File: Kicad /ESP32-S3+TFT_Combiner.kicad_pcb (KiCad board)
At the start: 2 copper layers, 98 x 55.9 mm, 6 parts, among them J1 Conn_01x04, J2 Conn_01x14, J3 Conn_01x22, J4 Conn_01x22, J5 Conn_01x22, J6 Conn_01x22

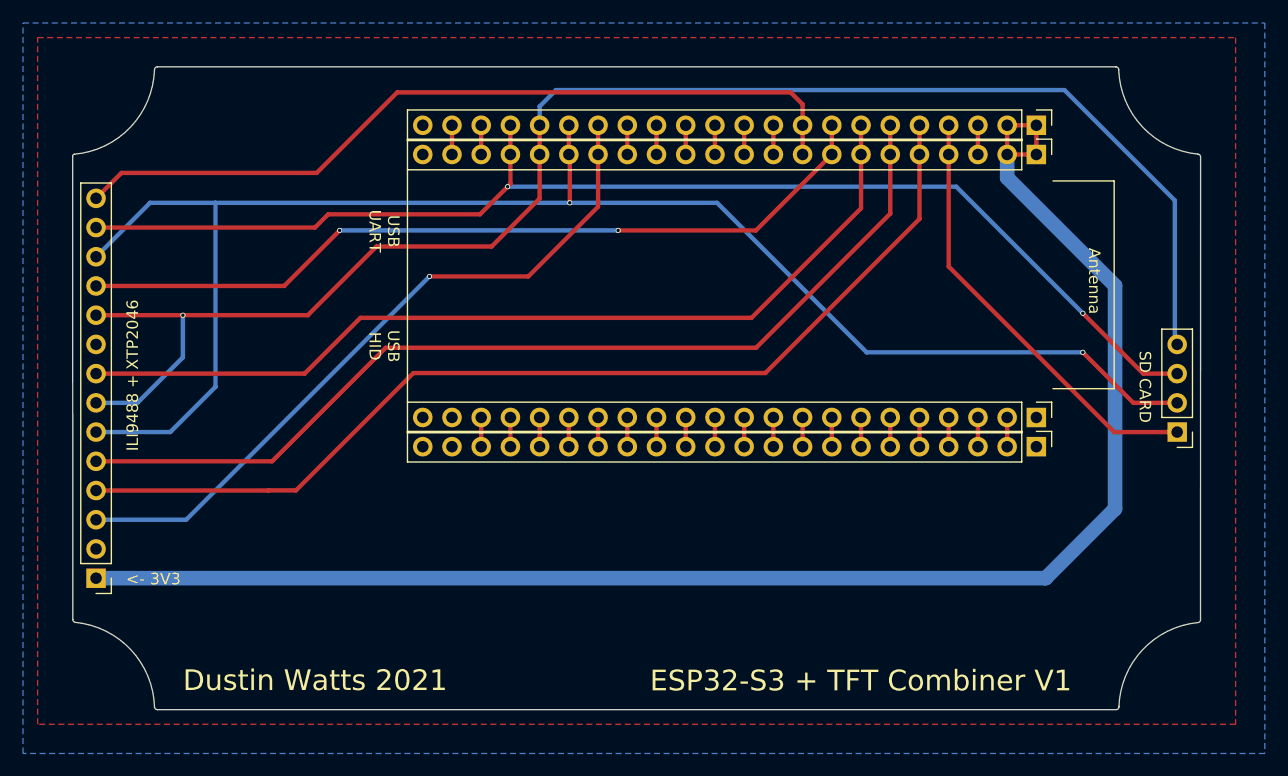
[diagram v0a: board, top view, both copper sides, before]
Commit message: Updated Silkscreen
Added pin numbering and correct a spelling mistake (XTP2040 = XPT2046)
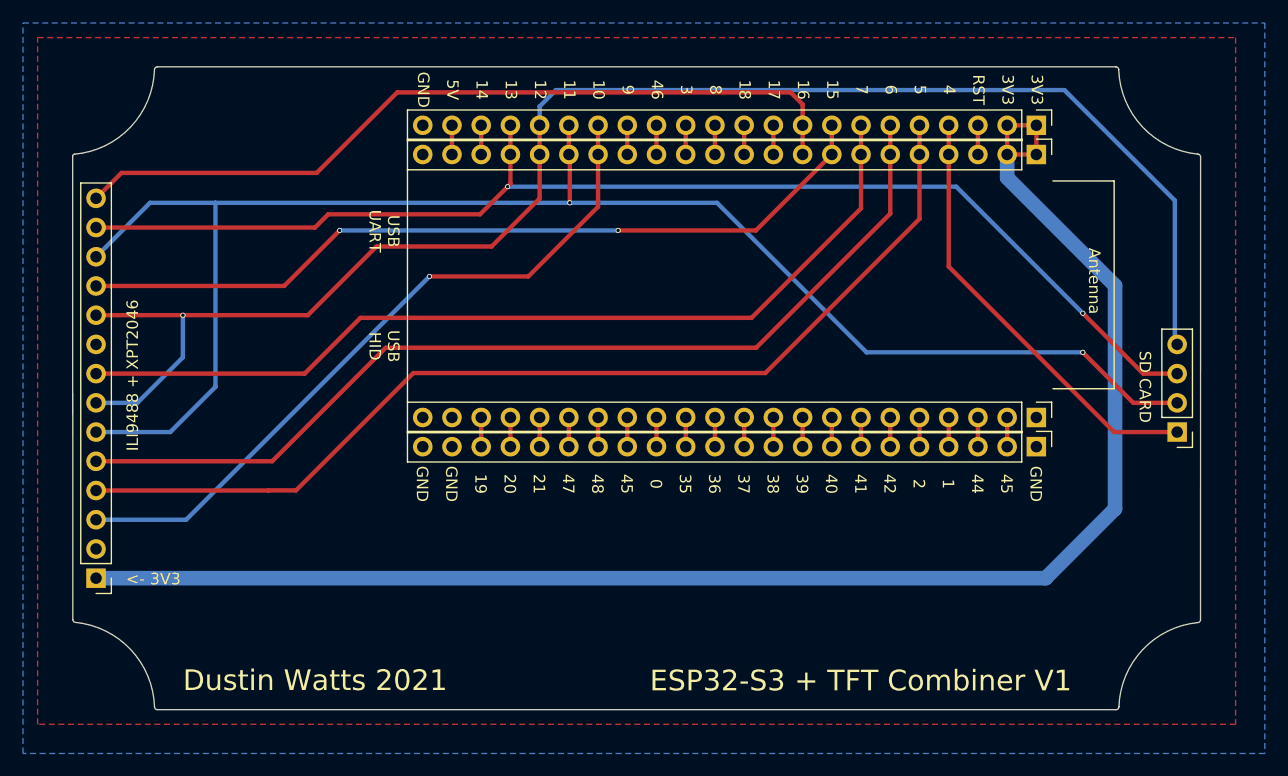
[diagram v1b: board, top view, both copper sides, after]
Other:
- board text added: "0"
- board text added: "1"
- board text added: "10"
- board text added: "11"
- board text added: "12"
- board text added: "13"
- board text added: "14"
- board text added: "15"
- board text added: "16"
- board text added: "17"
- board text added: "18"
- board text added: "19"
- board text added: "2"
- board text added: "20"
- board text added: "21"
- board text added: "3"
- board text added: "35"
- board text added: "36"
- board text added: "37"
- board text added: "38"
- board text added: "39"
- board text added: "3V3"
- board text added: "4"
- board text added: "40"
- board text added: "41"
- board text added: "42"
- board text added: "44"
- board text added: "45"
- board text added: "46"
- board text added: "47"
- board text added: "48"
- board text added: "5"
- board text added: "5V"
- board text added: "6"
- board text added: "7"
- board text added: "8"
- board text added: "9"
- board text added: "GND"
- board text added: "ILI9488 + XPT2046"
- board text added: "RST"
- board text removed: "ILI9488 + XTP2046"
